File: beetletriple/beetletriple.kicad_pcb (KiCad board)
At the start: 4 copper layers, 80 x 64 mm, 72 parts, among them J1 Power IN, J2 motor_out, J3 motor_out, J4 motor_out, J5 input_c1, J6 input_c2, J7 input_c3, J8 output_c4, J9 output_c5, Q1 IRF8313PBF, Q2 IRF8313PBF, Q3 IRF8313PBF, Q4 IRF8313PBF, Q5 IRF8313PBF, Q6 IRF8313PBF, U1 TPS54331DR, U11 FAN7388MX, U12 FAN7388MX, U2 HT7550-1, U3 ATtiny1617-M

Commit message: misc updates
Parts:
- added J10: soicbite programming connector, beetletriple:SOIC_clipProgSmall, F.Cu at (177.5, 110.5)
- moved C2 42.9 mm to (128.1, 83.6), turned to -90 degrees
- moved C1 40.4 mm to (148.0, 83.1), turned to -90 degrees
- moved U2 7.51 mm to (147.3, 120.6), turned to 180 degrees
- moved D10 5.60 mm to (175.0, 125.9), turned to 180 degrees
- moved R15 5.60 mm to (171.0, 125.9), turned to 180 degrees
- moved J1 4.96 mm to (107.0, 126.0)
- moved F1 4.80 mm to (121.2, 131.5)
- moved C3 4.61 mm to (151.5, 130.0)
- moved C4 4.61 mm to (163.5, 130.0)
- moved C6 4.61 mm to (120.0, 122.5), turned to 0 degrees
- moved D9 4.10 mm to (175.0, 123.9), turned to 180 degrees
- moved R14 4.10 mm to (171.0, 123.9), turned to 180 degrees
- moved U3 4.03 mm to (141.5, 109.5)
- moved REF** 3.61 mm to (99.5, 133.5)
- moved C7 3.42 mm to (151.6, 120.5)
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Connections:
- D10 pad 1: Net-(D10-Pad1) -> GND
- D10 pad 2: /MCU/BLINKY2 -> Net-(D10-Pad2)
- D8 pad 1: Net-(D8-Pad1) -> GND
- D8 pad 2: VLOGIC -> Net-(D8-Pad2)
- D9 pad 1: Net-(D9-Pad1) -> GND
- D9 pad 2: /MCU/BLINKY1 -> Net-(D9-Pad2)
- R13 pad 1: GND -> Net-(D8-Pad2)
- R13 pad 2: Net-(D8-Pad1) -> VLOGIC
- R14 pad 1: GND -> Net-(D9-Pad2)
- R14 pad 2: Net-(D9-Pad1) -> /MCU/BLINKY1
- R15 pad 1: GND -> Net-(D10-Pad2)
- R15 pad 2: Net-(D10-Pad1) -> /MCU/BLINKY2
- U3 pad 21: /MCU/BLINKY1 -> /MCU/BLINKY2
- U3 pad 22: /MCU/BLINKY2 -> /MCU/BLINKY1
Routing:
- net VBEC: track 26.1 -> 141.6 mm, vias 0 -> 8
- net VLOGIC: track 5.61 -> 90.6 mm, vias 0 -> 4
- net /MCU/RXIN3: track 0.00 -> 44.9 mm, vias 0 -> 2
- net /MCU/BLINKY2: track 0.00 -> 41.5 mm, vias 0 -> 2
- net /MCU/TXDEBUG: track 0.00 -> 41.5 mm, vias 0 -> 3
- net /MCU/RXIN1: track 0.00 -> 41.0 mm, vias 0 -> 2
- net /MCU/BLINKY1: track 0.00 -> 40.4 mm, vias 0 -> 2
- net /MCU/RXIN2: track 0.00 -> 40.3 mm, vias 0 -> 2
- net /MCU/UPDI: track 0.00 -> 37.7 mm, vias 0 -> 3
- net /MCU/SERVO1: track 0.00 -> 30.5 mm, vias 0 -> 2
- net GND: track 94.1 -> 123.7 mm, vias 33 -> 35
- net /MCU/SERVO2: track 0.00 -> 29.0 mm, vias 0 -> 2
- net VBAT_IN_1: track 22.1 -> 0.00 mm
- net VBAT: track 52.9 -> 38.8 mm, vias 45 -> 40
- net MOTOR3L2: track 25.4 -> 20.1 mm
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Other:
- board size 80 x 64 mm -> 82 x 61 mm

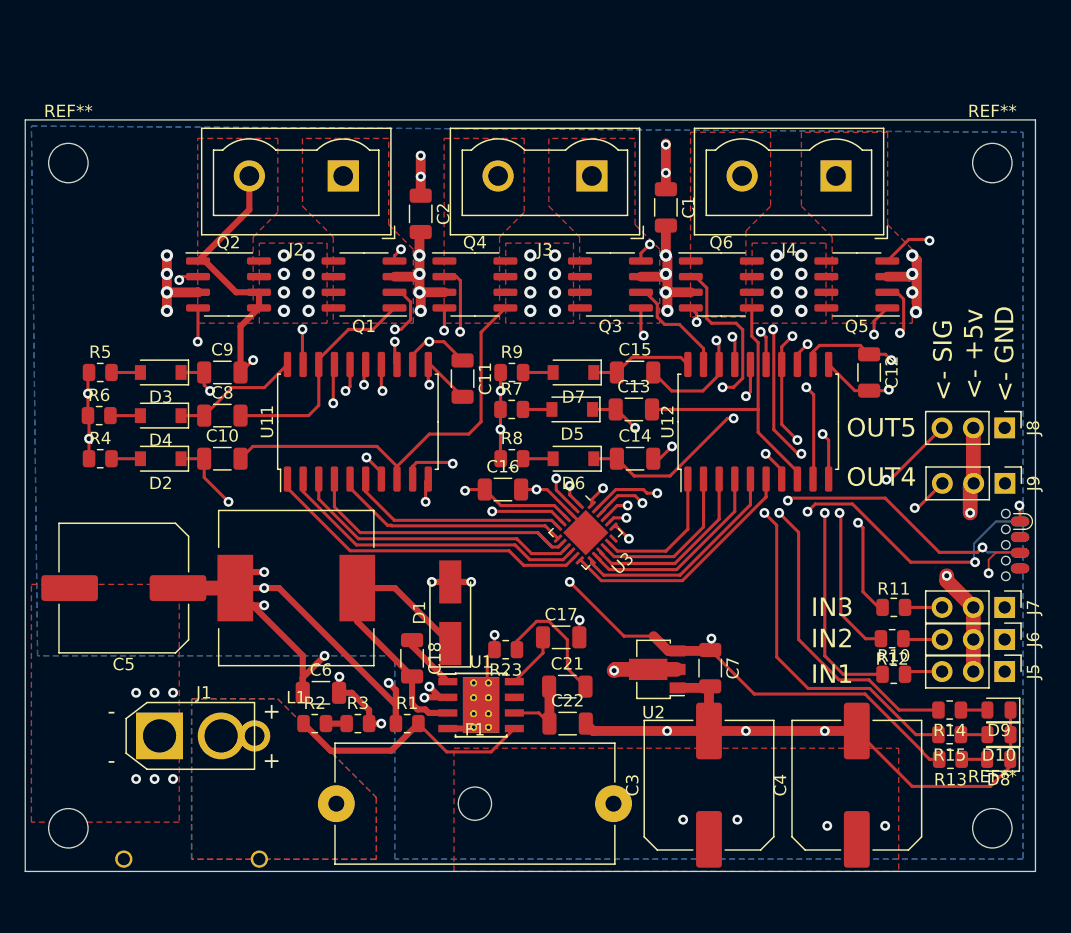
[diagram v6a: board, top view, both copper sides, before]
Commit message: Shunt current sensor. Many improvements, layout updates
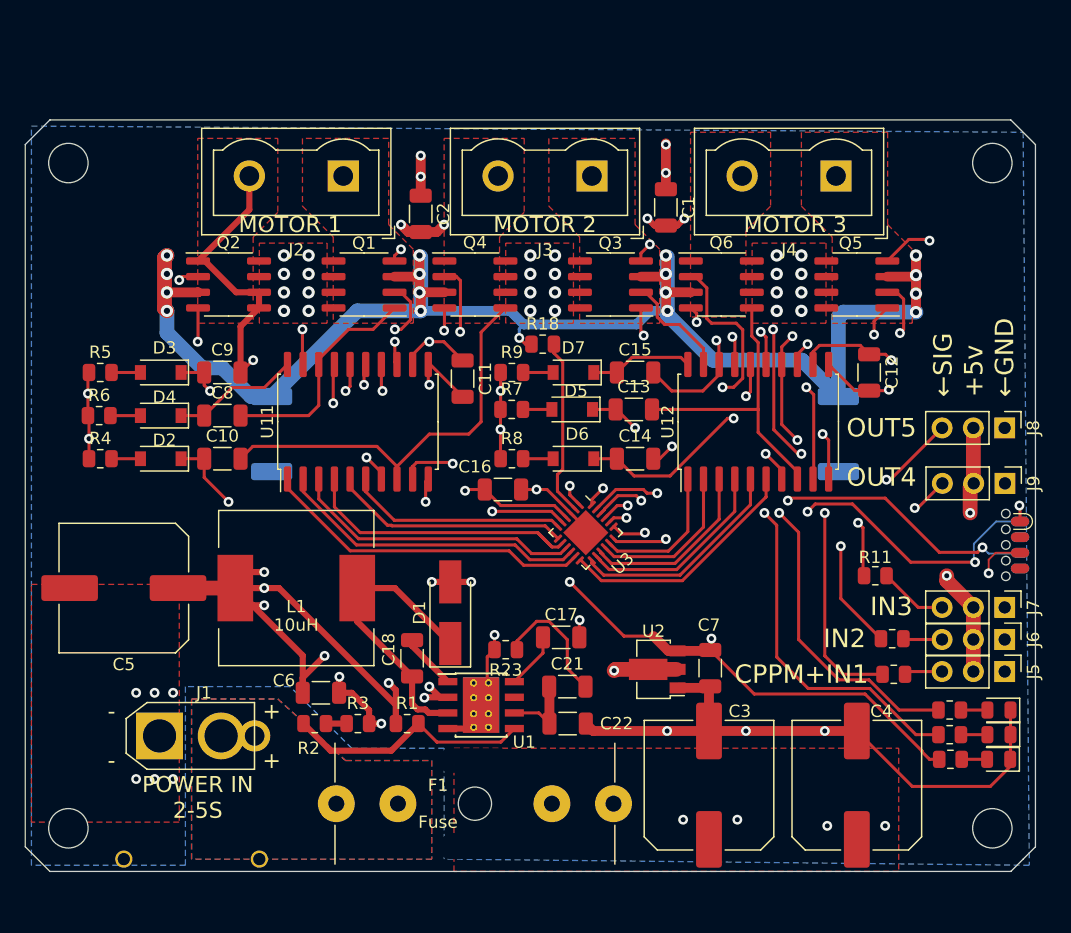
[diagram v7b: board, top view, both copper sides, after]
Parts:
- added R16: 0.01R shunt, Resistor_SMD:R_2512_6332Metric_Pad1.40x3.35mm_HandSolder, B.Cu at (162.0, 101.5)
- added R17: 0.01R shunt, Resistor_SMD:R_2512_6332Metric_Pad1.40x3.35mm_HandSolder, B.Cu at (116.0, 101.5)
- added R18: 1.5k, Resistor_SMD:R_0805_2012Metric, F.Cu at (138.0, 94.2)
- F1: footprint Fuse:Fuseholder_Cylinder-5x20mm_Schurter_0031_8201_Horizontal_Open -> beetletriple:fuseholder_flexible
- moved R11 2.98 mm to (165.0, 113.0)
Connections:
- Q1 pad 3: GND -> /Drivers/GNDSHUNT
- Q2 pad 3: GND -> /Drivers/GNDSHUNT
- Q3 pad 3: GND -> /Drivers/GNDSHUNT
- Q4 pad 3: GND -> /Drivers/GNDSHUNT
- Q5 pad 3: GND -> /Drivers/GNDSHUNT
- Q6 pad 3: GND -> /Drivers/GNDSHUNT
- U3 pad 18: unconnected-(U3-Pad18) -> /MCU/RXIN2
- U3 pad 2: /MCU/RXIN2 -> CURRENTSENSE
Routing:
- net /Drivers/GNDSHUNT: track 0.00 -> 130.4 mm, vias 0 -> 17
- net GND: track 123.7 -> 95.6 mm, vias 35 -> 23
- net CURRENTSENSE: track 0.00 -> 14.5 mm
- net /MCU/RXIN2: track 40.3 -> 27.7 mm
- net /MCU/RXIN3: track 44.9 -> 41.4 mm
- net Net-(J7-Pad3): track 3.01 -> 5.57 mm
- net /Power/REG_SENSE: track 20.7 -> 20.0 mm
- added copper zone on B.Cu, net GND
- added copper zone on In1.Cu, net VBAT
- removed copper zone on In1.Cu, net GND
- removed copper zone on In2.Cu, net GND
- removed copper zone on B.Cu, net VBAT
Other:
- outline, holes or cut-outs redrawn
- board text added: "+5v"
- board text added: "CPPM+IN1"
- board text added: "Fuse"
- board text added: "MOTOR 1"
- board text added: "MOTOR 2"
- board text added: "MOTOR 3"
- board text added: "POWER IN 2-5S"
- board text added: "←GND"
- board text added: "←SIG"
- board text removed: "<- +5v"
- board text removed: "<- GND"
- board text removed: "<- SIG"
- board text removed: "IN1"

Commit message: add lcsc part numbers
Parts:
- D9: value Red -> Green
